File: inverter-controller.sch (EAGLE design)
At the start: 134 parts, among them IC1 STM32F334C8T6, IC2 SY7152ABC, IC3 LMV358MMX, IC4 LMV358MMX, IC5 SY7152ABC, J1 621006245821, J2 61300211121, X1 0289-9066**15EDGVC-3.81-02P-14, X2 0289-9066**15EDGVC-3.81-02P-14, X4 0289-9066**15EDGVC-3.81-02P-14, X6 1365-16, Y1 NX2016SA-32M

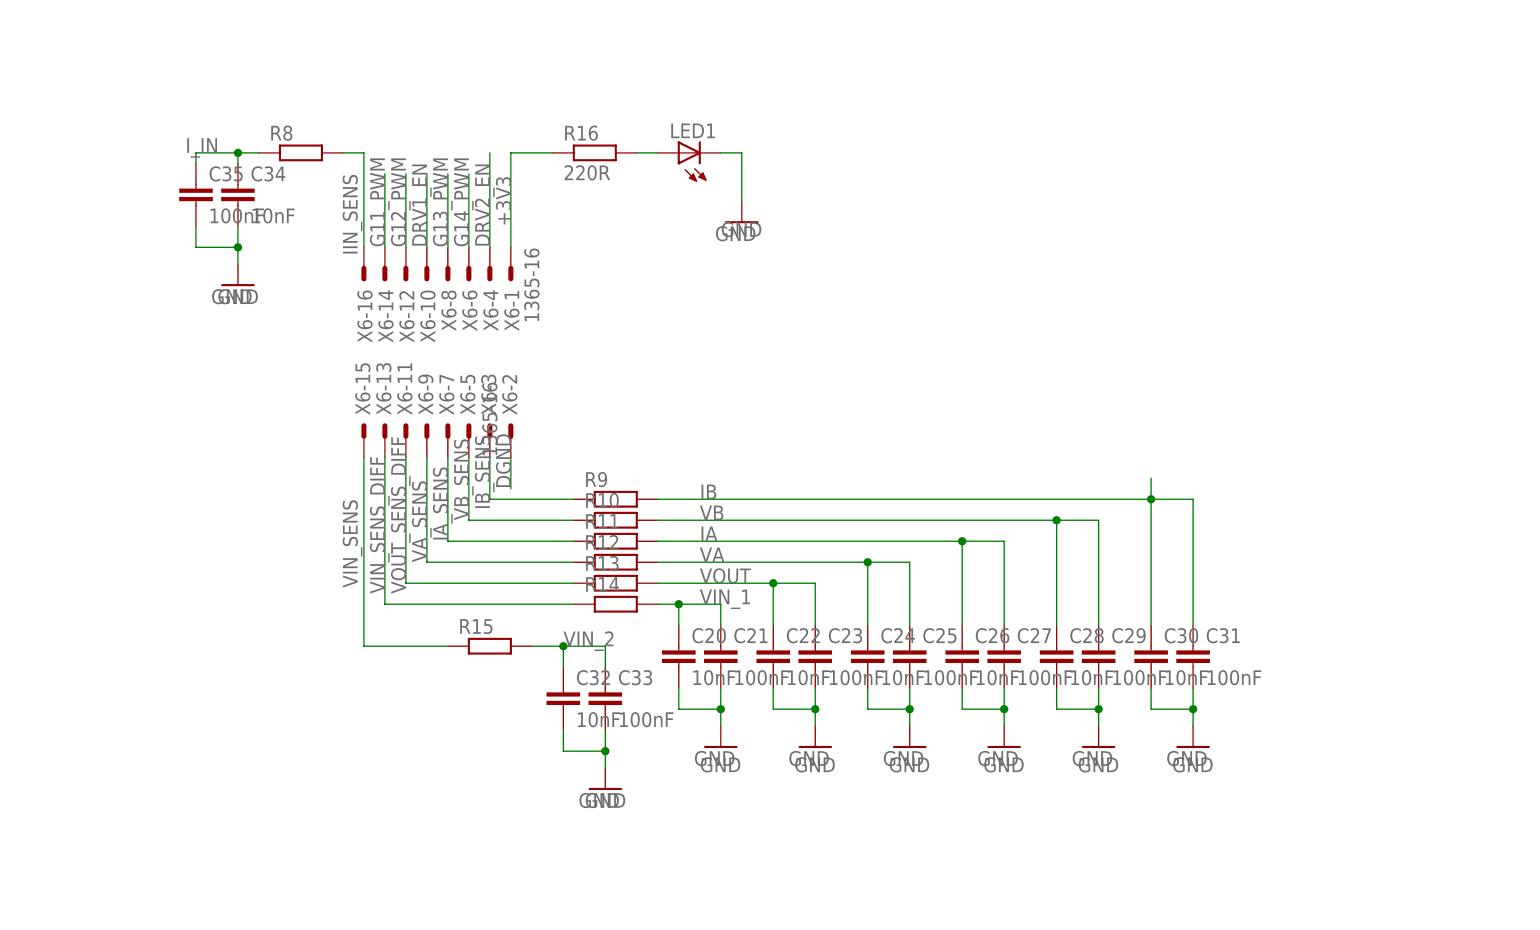
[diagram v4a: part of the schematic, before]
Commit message: Akim olcumleri icin gerilim bolucu direncler eklendi.
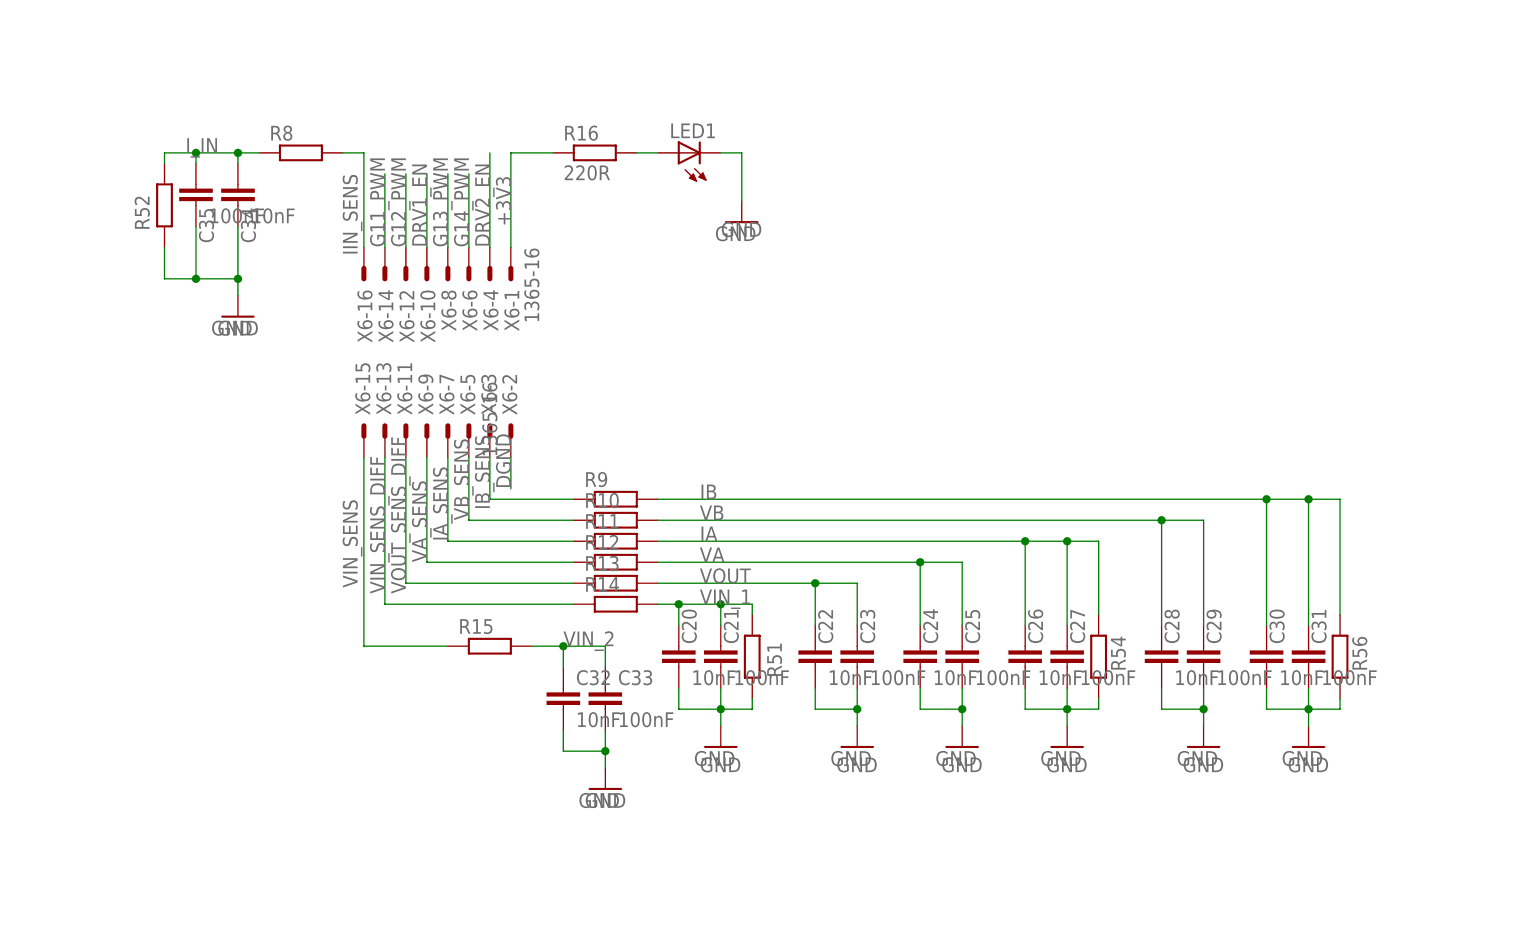
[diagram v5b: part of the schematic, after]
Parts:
- added R51, R52, R54, R56: (no value), rcl:R-EU_R0603E
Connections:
- net GND: now also R51.1, R52.1, R54.1, R56.1
- net IA: now also R54.2
- net IB: now also R56.2
- net I_IN: now also R52.2
- net VIN_1: now also R51.2
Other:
- moved on the sheet: C22, C23, C24, C25, C26, C27, C28, C29, C30, C31

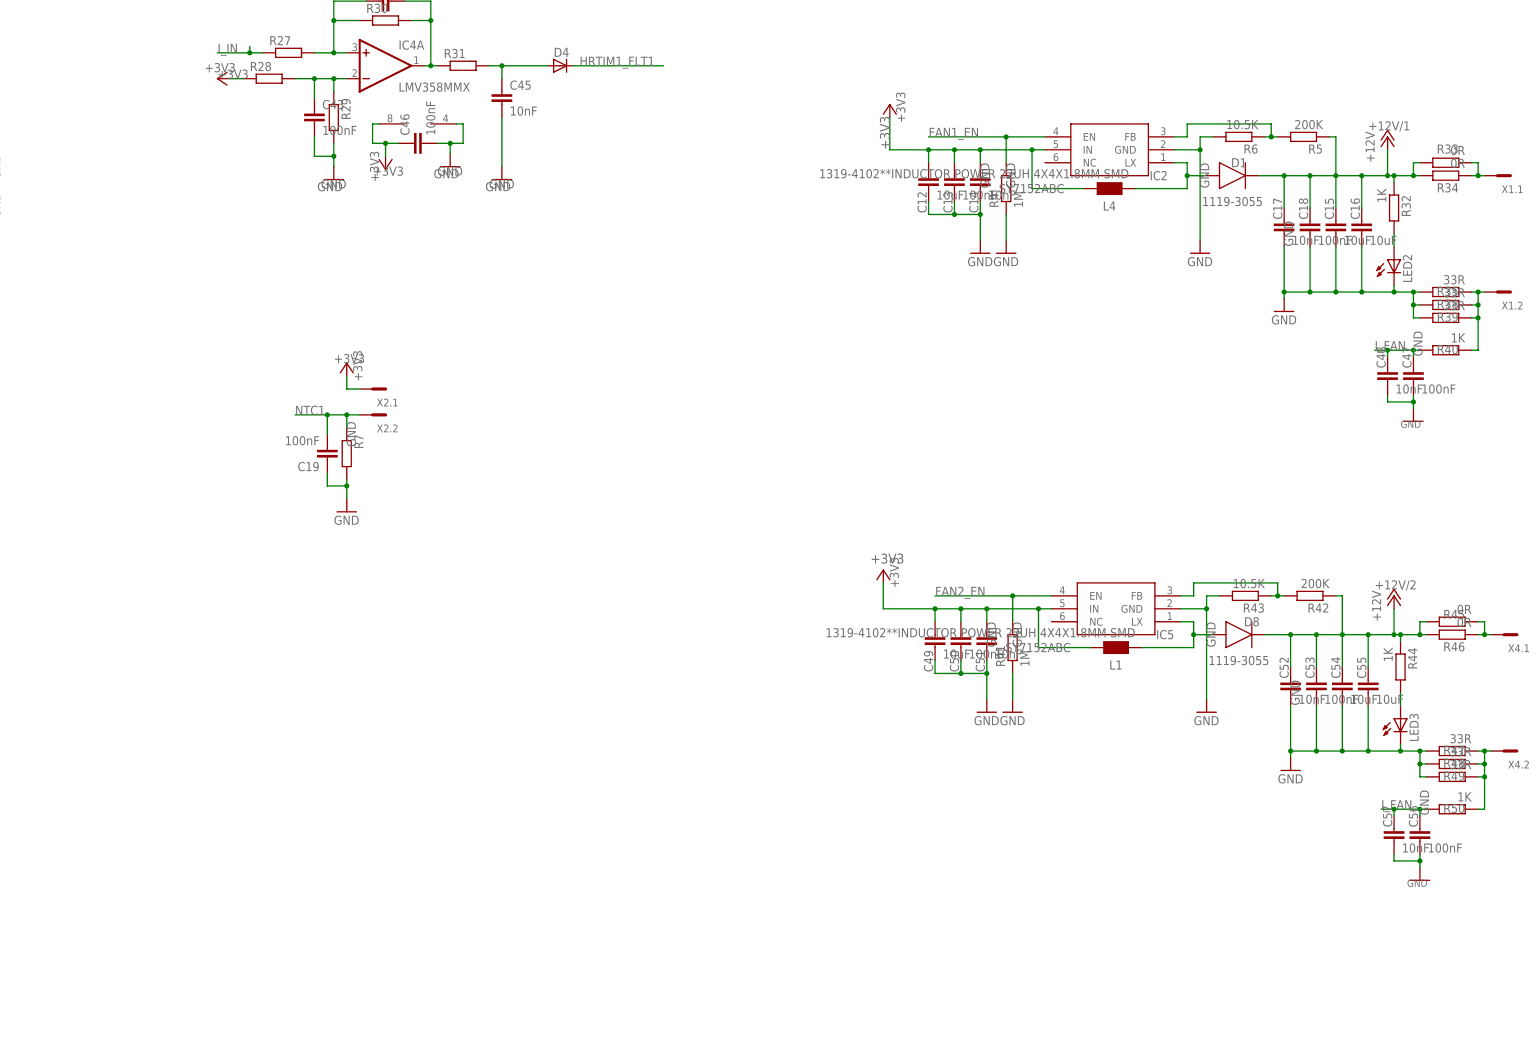
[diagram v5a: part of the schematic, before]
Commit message: Fan beslemelerinden bir tanesi silindi.
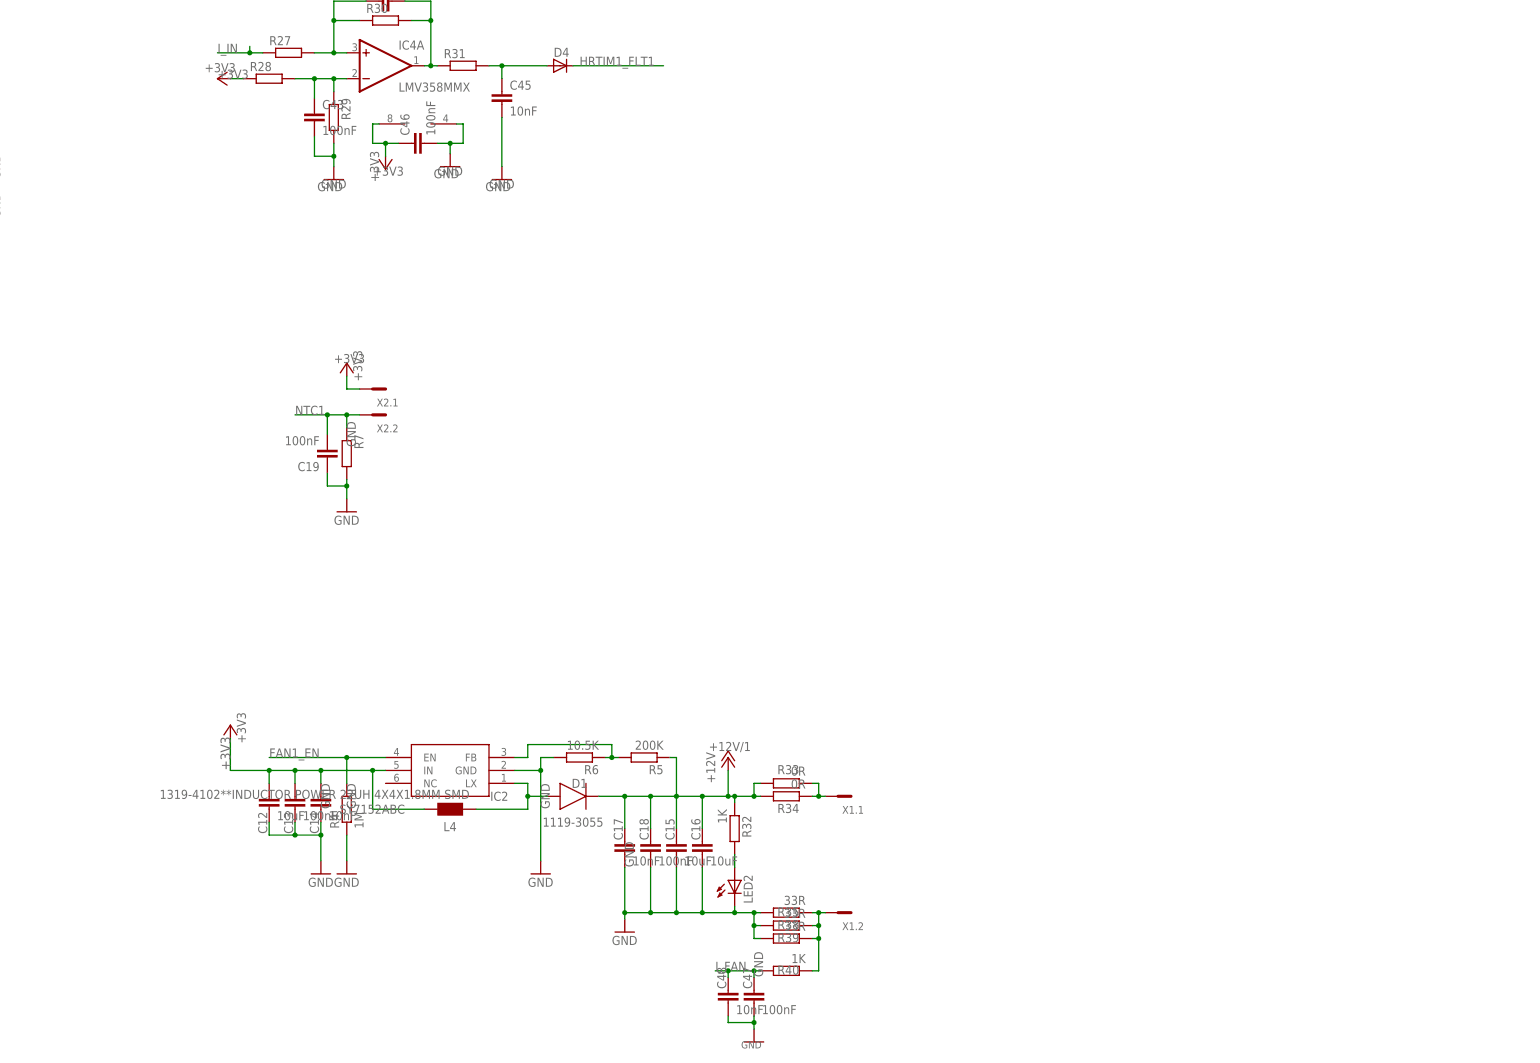
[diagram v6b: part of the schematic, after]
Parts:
- removed C49, C54, C55: 10uF, rcl:C-EUC0603E
- removed C50, C53, C56: 100nF, rcl:C-EUC0603E
- removed C51, C52, C57: 10nF, rcl:C-EUC0603E
- removed D8: 1119-3055, Diode:DIODEDO-214AC(SMA)
- removed IC5: SY7152ABC, SY7152ABC:SY7152ABC
- removed L1: 1319-4102**INDUCTOR POWER 22UH 4X4X1.8MM SMD, wuerth-elektronik:WE-PD2_S
- removed LED3: (no value), adafruit:LEDCHIP-LED0805
- removed R41: 1M, rcl:R-EU_R0603E
- removed R42: 200K, rcl:R-EU_R0603E
- removed R43: 10.5K, rcl:R-EU_R0603E
- removed R44, R50: 1K, rcl:R-EU_R0603E
- removed R45, R46: 0R, rcl:R-EU_R0603E
- removed R47, R48, R49: 33R, rcl:R-EU_R0603E
- removed X4: 0289-9066**15EDGVC-3.81-02P-14, con-phoenix-381_l:MCV2
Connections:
- removed net +12V/2: C52.1, C53.1, C54.1, C55.1, D8.C, R42.1, R44.1, R45.2, R46.2
- removed net N$36: D8.A, IC5.LX, L1.1
- removed net N$40: IC5.FB, R42.2, R43.1
- removed net N$41: R45.1, R46.1, X4.1.SK
- removed net N$42: R47.1, R48.1, R49.1, R50.1, X4.2.SK
- removed net N$43: LED3.A, R44.2
- net +3V3: no longer C49.1, C50.1, C51.1, IC5.IN, L1.2
- net FAN2_EN: no longer IC5.EN, R41.2
- net GND: no longer C49.2, C50.2, C51.2, C52.2, C53.2, C54.2, C55.2, C56.2, C57.2, IC5.GND, LED3.C, R41.1, R43.2, R47.2, R48.2, R49.2
- net I_FAN: no longer C56.1, C57.1, R50.2
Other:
- moved on the sheet: C12, C13, C14, C15, C16, C17, C18, C47, C48, D1, IC2, L4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

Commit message: RS485 eklendi.
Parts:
- added C49, C50: 1019-3166**CAP 0603 CER 100nF 16V %10 X7R (AbC), rcl:C-EUC0603
- added C51, C53: 1019-3168","CAP 0805 CER 2.2uF 16V %10 X7R (AbC), rcl:C-EUC0805
- added C52: 0019-3020","CAP TH CER 470pF 3kV Y5P %10 85C F=7.5 D=8.5, rcl:C-EU050-055X075
- added C60, C61: 1200920378**CAP 0603 CER 100p 50V%5 NP0, rcl:C-EUC0603
- added C66: NC, rcl:C-EUC0603
- added D10: 1119-3034_ESD Protection Diode for CANBUS NXP PESD2CAN SOT23, diode:DIODE-2CAPACITANCESOT23
- added IC10: ISO3082, enko:ISO3082
- added L1: 1319-4025","INDUCTOR SMD 0805 4.7uH 500mA CL2012C-4R7M Core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, rcl:R-EU_R0805
- added L6: 1319-4002_ACM2012 SMD Common Mode Filter, enko:ACM2012-900--2P-T002
- added LED4: 1209-0004**LED GREEN CLEAR THIN 0805 SMD, led:LEDCHIP-LED0805
- added Q17: 1039-2335","DC-DC Converter 5V to 5V 1W RFMM-0505S, enko:RFMM-0505S
- added R41: 1029-2232**RES 0603 120R %1, rcl:R-EU_R0603
- added R48: 1409-0025**RES 0603 470R %5 1/16W, rcl:R-EU_R0603
- added R65, R66, R69: 1029-2003**RES 0603 10R %1, rcl:R-EU_R0603
- added TP11, TP4, TP5, TP6, TP7, TP8: PTR1TP18R, testpad:PTR1TP18R
- added X3: 0289-9068**15EDGVC-3.81-03P-14, con-phoenix-381_l:MCV3
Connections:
- new net +5V: C51.1, L1.1
- new net 485A_PORT: D10.A1, R41.1, R69.1, X3.2.SK
- new net 485B_PORT: D10.A2, R41.2, R66.2, X3.1.SK
- new net 485G_PORT1: C66.1, R65.2, X3.3.SK
- new net N$24: LED4.A, R48.2
- new net N$41: C61.1, IC10.A, L6.2, TP8.TP
- new net N$42: L6.4, R66.1
- new net N$57: L6.3, R69.2
- new net N$73: C60.2, IC10.B, L6.1, TP7.TP
- new net N$80: C52.1, L1.2, Q17.VIN+
- new net RS485_DIR: IC1.PB3, IC10.DE, IC10.RE, TP5.TP
- new net RS485_ISO_5V: C50.2, C52.2, C53.1, IC10.VCC2, Q17.VOUT+
- new net RS485_ISO_GND: C50.1, C53.2, C60.1, C61.2, C66.2, D10.C, IC10.GND2-1, IC10.GND2-2, IC10.GND2-3, Q17.VOUT-, R65.1
- new net RS485_LED: IC1.PB4, LED4.C, TP11.TP
- new net RS485_RX: IC1.PB11, IC10.R, TP4.TP
- new net RS485_TX: IC1.PB10, IC10.D, TP6.TP
- net +3V3: now also C49.2, IC10.VCC1, R48.1
- net GND: now also C49.1, C51.2, IC10.GND1-1, IC10.GND1-2, IC10.GND1-3, Q17.VIN-
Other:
- note added: "Bus-Pin ESD Protection – 12-kV HBM Between Bus Pins and GND2 – 6-kV HBM Between Bus Pins and GND1 ISO3082 de dahili varmis. Yani TVS eklemeye gerek yok"
- note added: "Fail-safe Receiver for Bus Open, Short ISO3082'de Fail-Safe var, A'ya pullup ve B'ye pulldown eklemeye gerek yok"
- note added: "RS485"
- note added: "SGND ile X10-3 arasindaki 100ohm luk direnc standartlarda olan bir degerdir. Opsiyonel olarak eklenmistir."
- note added: "İzolasyon"
- note added: "İzole taraf(sağ) için lokal groundlama yapilacak"

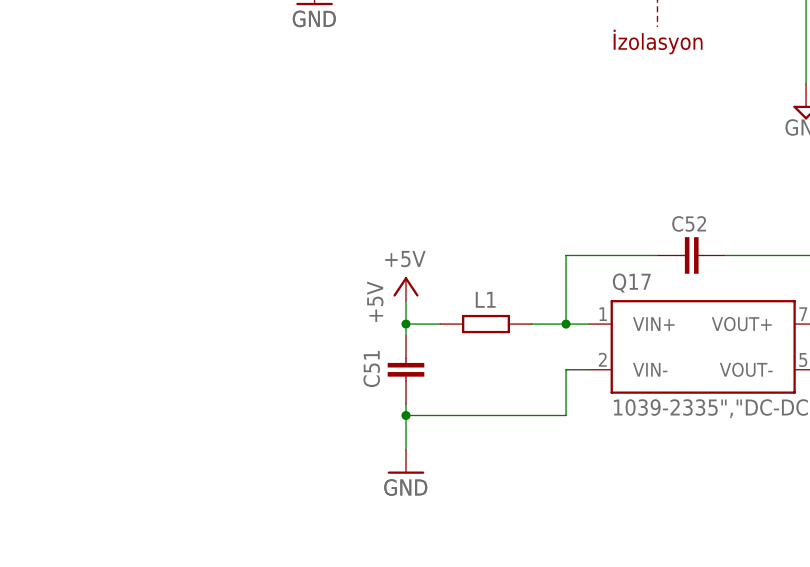
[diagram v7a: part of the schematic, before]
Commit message: RS485 DC-DC besleme gerilimi 3V yapildi.
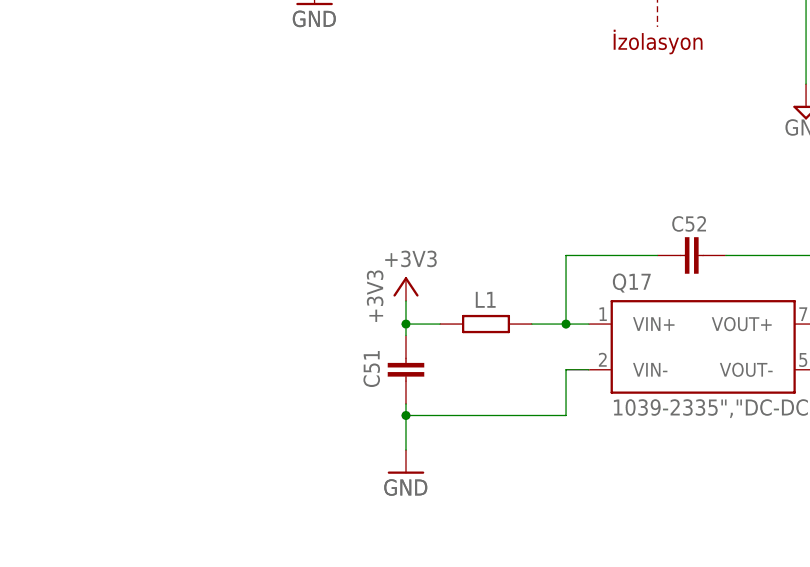
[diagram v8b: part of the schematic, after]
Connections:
- removed net +5V: C51.1, L1.1
- net +3V3: now also C51.1, L1.1
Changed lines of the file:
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@@
 <part name="C53" library="rcl" deviceset="C-EU" device="C0805" value="1019-3168&quot;,&quot;CAP 0805 CER 2.2uF 16V %10 X7R (AbC)"/>
 <part name="L1" library="rcl" deviceset="R-EU_" device="R0805" value="1319-4025&quot;,&quot;INDUCTOR SMD 0805 4.7uH 500mA CL2012C-4R7M Core Master"/>
-<part name="P+14" library="supply1" deviceset="+5V" device=""/>
 <part name="SUPPLY5" library="supply2" deviceset="+5V/4" device=""/>
 <part name="SUPPLY7" library="supply2" deviceset="GND4" device=""/>
@@
 <part name="GND32" library="supply1" library_urn="urn:adsk.eagle:library:371" deviceset="GND" device=""/>
 <part name="+3V16" library="supply1" deviceset="+3V3" device=""/>
+<part name="+3V17" library="supply1" deviceset="+3V3" device=""/>
 </parts>
 <sheets>
@@
 <attribute name="NAME" x="391.16" y="172.4914" size="1.778" layer="95" rot="R180"/>
 </instance>
-<instance part="P+14" gate="1" x="381" y="173.99" smashed="yes">
-<attribute name="VALUE" x="378.46" y="168.91" size="1.778" layer="96" rot="R90"/>
-</instance>
 <instance part="SUPPLY5" gate="G$1" x="448.31" y="173.99" smashed="yes">
 <attribute name="VALUE" x="444.5" y="177.165" size="1.778" layer="96"/>
@@
 <instance part="+3V16" gate="G$1" x="462.28" y="187.96" smashed="yes">
 <attribute name="VALUE" x="459.74" y="182.88" size="1.778" layer="96" rot="R90"/>
+</instance>
+<instance part="+3V17" gate="G$1" x="381" y="173.99" smashed="yes">
+<attribute name="VALUE" x="378.46" y="168.91" size="1.778" layer="96" rot="R90"/>
 </instance>
 </instances>
@@
 <label x="459.74" y="187.96" size="1.778" layer="95"/>
 <pinref part="+3V16" gate="G$1" pin="+3V3"/>
+</segment>
+<segment>
+<pinref part="C51" gate="G$1" pin="1"/>
+<wire x1="381" y1="171.45" x2="381" y2="168.91" width="0.1524" layer="91"/>
+<wire x1="381" y1="168.91" x2="381" y2="167.64" width="0.1524" layer="91"/>
+<wire x1="384.81" y1="168.91" x2="381" y2="168.91" width="0.1524" layer="91"/>
+<junction x="381" y="168.91"/>
+<pinref part="L1" gate="G$1" pin="1"/>
+<label x="378.46" y="175.26" size="1.778" layer="95"/>
+<pinref part="+3V17" gate="G$1" pin="+3V3"/>
 </segment>
 </net>
@@
 </segment>
 </net>
-<net name="+5V" class="0">
-<segment>
-<pinref part="C51" gate="G$1" pin="1"/>
-<wire x1="381" y1="171.45" x2="381" y2="168.91" width="0.1524" layer="91"/>
-<wire x1="381" y1="168.91" x2="381" y2="167.64" width="0.1524" layer="91"/>
-<wire x1="384.81" y1="168.91" x2="381" y2="168.91" width="0.1524" layer="91"/>
-<junction x="381" y="168.91"/>
-<pinref part="L1" gate="G$1" pin="1"/>
-<label x="378.46" y="175.26" size="1.778" layer="95"/>
-<pinref part="P+14" gate="1" pin="+5V"/>
-</segment>
-</net>
